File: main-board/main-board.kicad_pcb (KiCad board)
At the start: 2 copper layers, 101 x 101 mm, 83 parts, among them J201 C10418, J401 TF-01A, J402 FH12-24S-0.5SH(55), Q102 Q_NPN_BCE, Q201 Q_NPN_BCE, Q202 Q_NPN_BCE, Q301 DMG1012T, SW101 RESET, U103 ESP-32s, U105 IPS6404L-SQ-SPN, U201 HT7333-A, U202 CH340E, U301 SX1308, U302 DW06D, U401 SN74LVC125ADBR, U402 RT9011-CMGJ6

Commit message: ALPHA 1
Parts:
- removed the TP101 at (157.7, 118.8)
- removed TP104: +5V, TestPoint:TestPoint_Pad_D1.0mm
- removed TP105: +3.3V, TestPoint:TestPoint_Pad_D1.0mm
- removed TP106: +3V3, TestPoint:TestPoint_Pad_D1.0mm
- removed TP107: +1V2, TestPoint:TestPoint_Pad_D1.0mm
- added TP201: +5V, TestPoint:TestPoint_Pad_D1.0mm, F.Cu at (101.0, 75.1)
- added TP202: +3.3V, TestPoint:TestPoint_Pad_D1.0mm, F.Cu at (105.7, 75.1)
- added TP301: +2V8, TestPoint:TestPoint_Pad_D1.0mm, F.Cu at (157.7, 118.8)
- added TP302: +1V2, TestPoint:TestPoint_Pad_D1.0mm, F.Cu at (163.4, 108.8)
- added TP401: +3V3, TestPoint:TestPoint_Pad_D1.0mm, F.Cu at (171.1, 121.5)
- renumbered BT301 to BT401, C104 to C101, C111 to C102, C407 to C301, C408 to C302, C409 to C303, C406 to C304, C404 to C305, C405 to C306, C301 to C401, C303 to C402, C304 to C403, C302 to C404, C401 to C501, C402 to C502, C403 to C503, D102 to D101, D301 to D401, J402 to J301, J401 to J501, L301 to L401, Q102 to Q101, Q301 to Q401, R116 to R101, R113 to R102, R118 to R103, R119 to R104, R405 to R301, R407 to R302, R408 to R303, R409 to R304, R410 to R305, R411 to R306, R406 to R307, R301 to R401, R302 to R402, R304 to R403, R306 to R404, R307 to R405, R303 to R406, R305 to R407, R401 to R501, R402 to R502, R403 to R503, R404 to R504, TP103 to TP101, TP301 to TP402, U103 to U101, U105 to U102, U402 to U301, U301 to U401, U302 to U402, U401 to U501

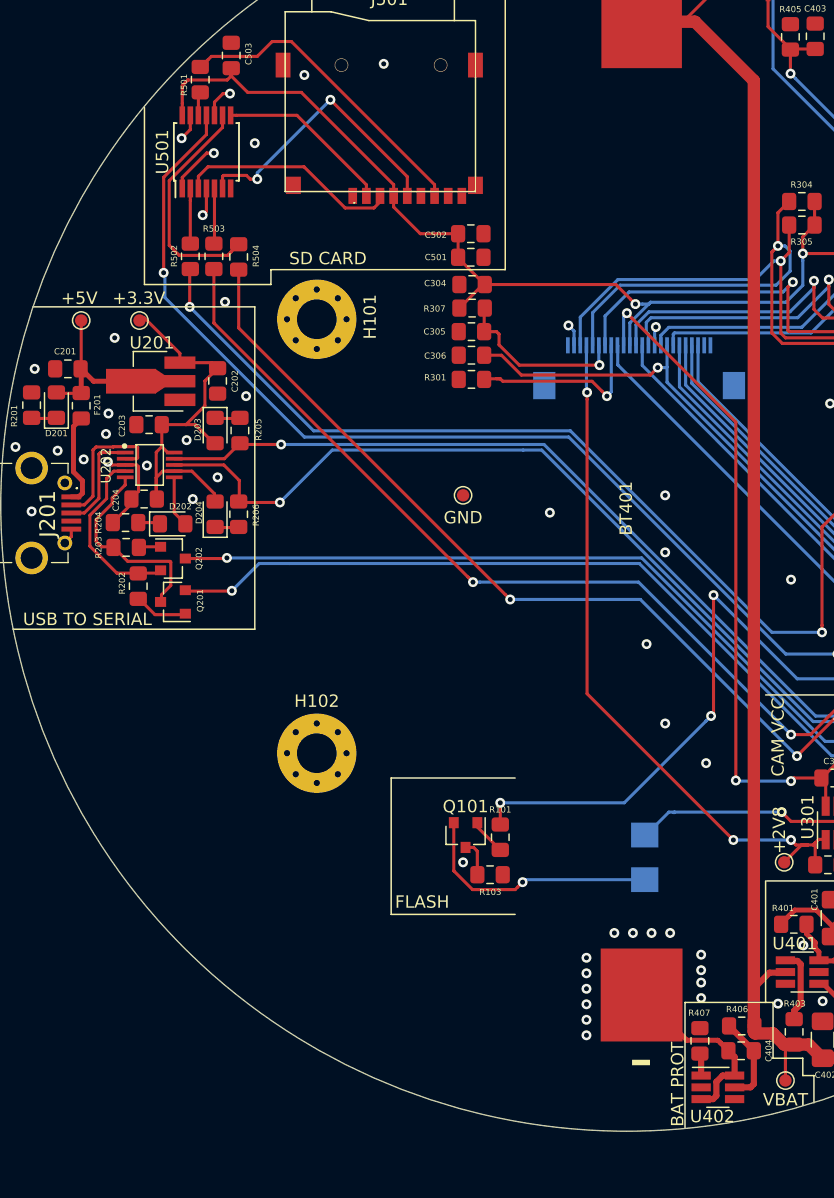
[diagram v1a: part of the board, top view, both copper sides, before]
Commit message: added battery charging
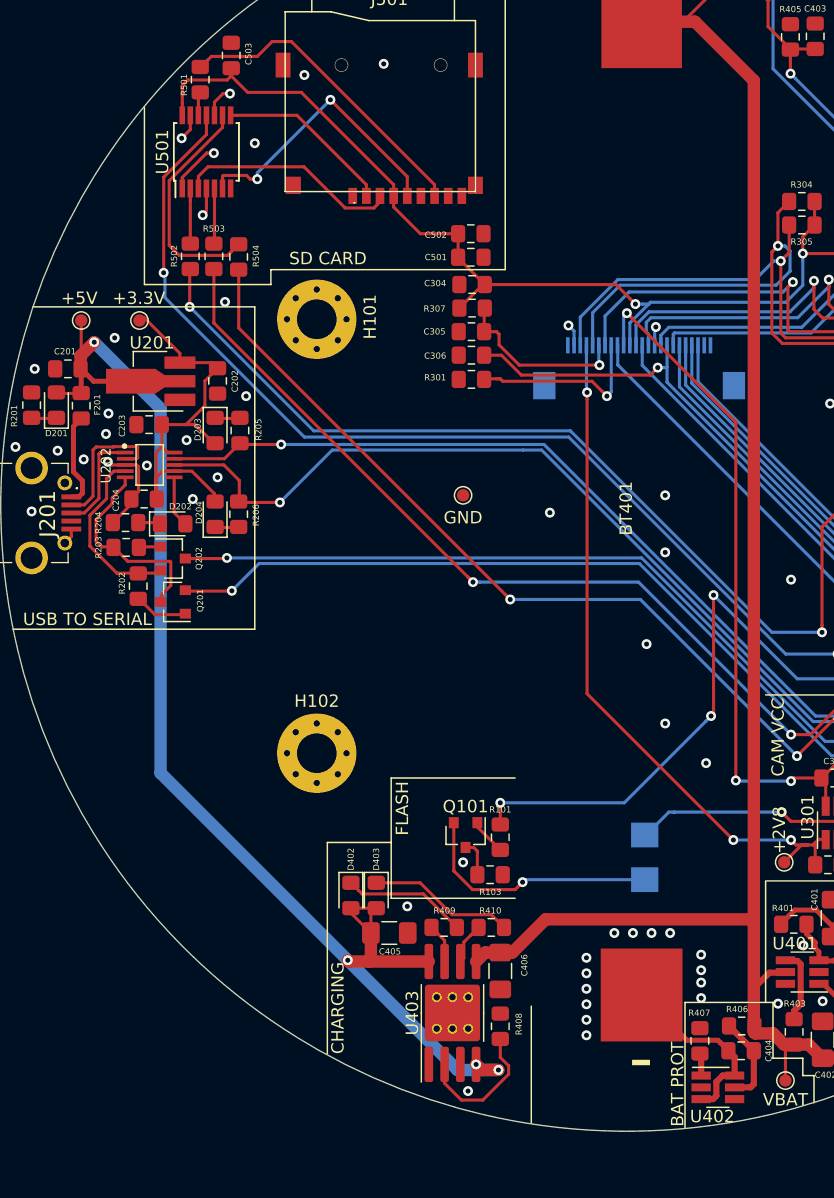
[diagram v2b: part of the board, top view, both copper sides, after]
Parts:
- added C405: 10uF, Capacitor_SMD:C_1206_3216Metric_Pad1.42x1.75mm_HandSolder, F.Cu at (125.8, 124.5)
- added C406: 10uF, Capacitor_SMD:C_1206_3216Metric_Pad1.42x1.75mm_HandSolder, F.Cu at (134.8, 127.6)
- added D402: RED, LED_SMD:LED_0805_2012Metric_Pad1.15x1.40mm_HandSolder, F.Cu at (122.8, 121.5)
- added D403: GREEN, LED_SMD:LED_0805_2012Metric_Pad1.15x1.40mm_HandSolder, F.Cu at (124.8, 121.5)
- added R408: 1k2, Resistor_SMD:R_0805_2012Metric_Pad1.15x1.40mm_HandSolder, F.Cu at (134.8, 132.0)
- added R409: 1k2, Resistor_SMD:R_0805_2012Metric_Pad1.15x1.40mm_HandSolder, F.Cu at (130.3, 124.0)
- added R410: 1k2, Resistor_SMD:R_0805_2012Metric_Pad1.15x1.40mm_HandSolder, F.Cu at (134.1, 124.0)
- added U403: TC4056A, Package_SO:SOP-8-1EP_4.57x4.57mm_P1.27mm_EP4.57x4.45mm_ThermalVias, F.Cu at (130.9, 130.9)
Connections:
- BT401 pad -: /BATTERY/BAT_GND -> GND
- C403 pad 2: /IO32 -> /BATTERY/BATTERY_READ
- C404 pad 2: /BATTERY/BAT_GND -> GND
- Q401 pad 1: /BAT_ST -> /BATTERY/START_READ
- Q401 pad 3: /IO32 -> /BATTERY/BATTERY_READ
- R405 pad 1: /IO32 -> /BATTERY/BATTERY_READ
- U402 pad 3: /BATTERY/BAT_GND -> GND
- U402 pad 6: /BATTERY/BAT_GND -> GND
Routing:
- net +5V: track 15.8 -> 110.3 mm, vias 0 -> 4
- net /BATTERY/VBAT: track 119.7 -> 143.5 mm
- net /BATTERY/BAT_GND: track 15.2 -> 0.00 mm
- net GND: track 29.0 -> 44.2 mm, vias 71 -> 73
- net Net-(D403-Pad1): track 0.00 -> 11.8 mm
- net Net-(R408-Pad1): track 0.00 -> 11.2 mm
- net Net-(D402-Pad1): track 0.00 -> 10.0 mm
- net Net-(R410-Pad2): track 0.00 -> 3.36 mm
- net Net-(R409-Pad2): track 0.00 -> 3.19 mm
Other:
- board text added: "CHARGING"
